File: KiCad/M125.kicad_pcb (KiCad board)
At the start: 2 copper layers, 28.9 x 13.7 mm, 20 parts, among them J1 Conn_01x04, J2 Conn_01x04, J3 Shelly, Q1 PMF250XNEX, U1 ESP32-PICO-MINI-02, U2 LMR16006+FB

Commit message: New PCB
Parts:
- added REF**: AJK, RevK:AJK, B.Cu at (88.0, 41.5)
- C3, C4, C5, D2, L1: moved to B.Cu
- moved D2 30.7 mm to (100.5, 42.3), turned to 180 degrees
- moved C3 23.5 mm to (96.2, 45.2), turned to 90 degrees
- moved L1 21.5 mm to (102.2, 45.5), turned to 180 degrees
- moved R1 13.2 mm to (112.2, 41.8), turned to 180 degrees
- moved R3 11.9 mm to (112.2, 43.2), turned to 180 degrees
- moved R5 11.2 mm to (99.6, 48.9)
- moved C5 11.2 mm to (103.7, 42.0), turned to -90 degrees
- moved R2 10.8 mm to (112.2, 44.8), turned to 180 degrees
- moved C2 10.8 mm to (94.0, 40.3), turned to 90 degrees
- moved R6 9.23 mm to (97.0, 48.9), turned to 0 degrees
- moved R4 8.25 mm to (94.9, 43.0), turned to -90 degrees
- moved C4 7.62 mm to (97.4, 42.0), turned to 90 degrees
- moved Q1 7.52 mm to (88.0, 49.5), turned to 90 degrees
- moved D1 7.22 mm to (112.2, 40.0), turned to 180 degrees
- moved C1 6.55 mm to (95.3, 47.2)
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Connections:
- U1 pad 12: unconnected-(U1-Pad12) -> DATA
- U1 pad 13: unconnected-(U1-Pad13) -> SEND
- U1 pad 18: NFCTX -> unconnected-(U1-Pad18)
- U1 pad 20: NFCRX -> unconnected-(U1-Pad20)
- U1 pad 21: DATA -> unconnected-(U1-Pad21)
- U1 pad 27: B -> NFCTX
- U1 pad 28: SEND -> NFCRX
- U1 pad 35: unconnected-(U1-Pad35) -> B
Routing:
- net +3V3: track 0.00 -> 41.0 mm, vias 0 -> 1
- net SEND: track 0.00 -> 10.8 mm, vias 0 -> 1
- net TX: track 0.00 -> 9.52 mm, vias 0 -> 1
- net B: track 0.00 -> 9.13 mm, vias 0 -> 1
- net RX: track 0.00 -> 8.70 mm, vias 0 -> 1
- net G: track 0.00 -> 8.58 mm, vias 0 -> 1
- net GPIO0: track 0.00 -> 7.65 mm
- net DC: track 0.00 -> 7.18 mm
- net NFCTX: track 0.00 -> 7.13 mm
- net R: track 0.00 -> 6.46 mm, vias 0 -> 1
- net Net-(D1-Pad3): track 0.00 -> 6.08 mm
- net EN: track 0.00 -> 4.58 mm, vias 0 -> 1
- net DATA: track 0.00 -> 4.55 mm, vias 0 -> 1
- net Net-(D1-Pad4): track 0.00 -> 4.53 mm
- net GND: track 0.00 -> 4.46 mm, vias 0 -> 1
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- added copper zone on B.Cu, net GND
- added copper zone on F.Cu, net GND
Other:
- board size 28.9 x 13.7 mm -> 29 x 13.6 mm
- board text added: "-33"
- board text added: "32"
- board text added: "3V3"
- board text added: "7"
- board text added: "8"
- board text added: "DATA"
- board text added: "DC"
- board text added: "M-125"
- board text added: "M-125 SCALES"
- board text added: "NFC"
- board text added: "NFC READER"
- board text added: "RGB: 22/19/21"
- board text added: "SEND"
- board text added: "⏚"
- board text removed: "RGB: 22/19/7"
- board text removed: "www.me.uk"

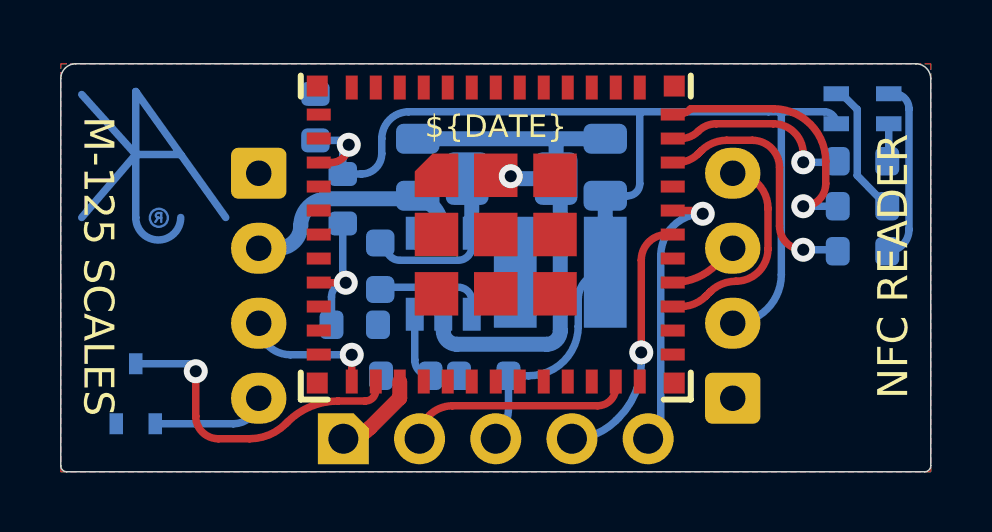
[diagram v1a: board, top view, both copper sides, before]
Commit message: Tidy PCB for placement of regulator parts
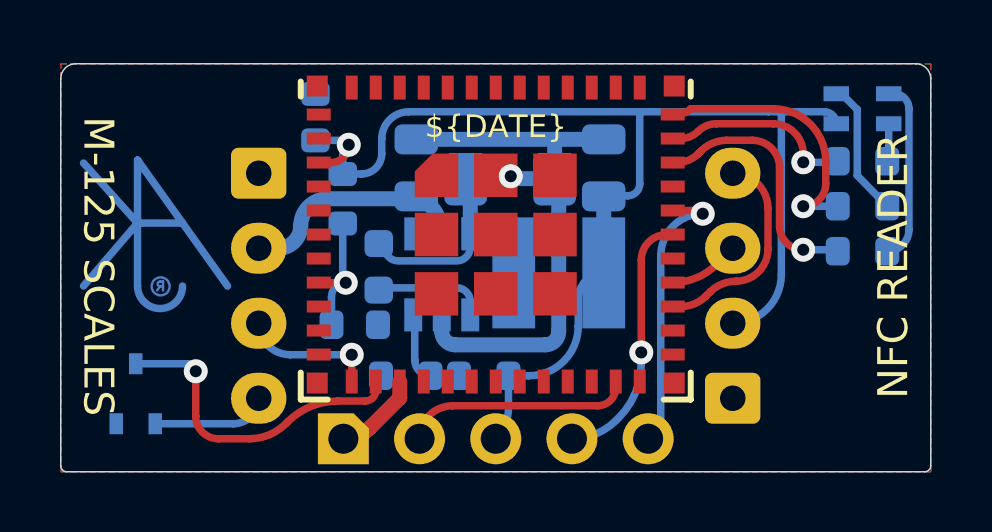
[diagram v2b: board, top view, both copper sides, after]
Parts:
- removed REF**: AJK, RevK:AJK
- added Logo1: AJK, RevK:AJK, B.Cu at (88.1, 43.8)
- C3: value 0.1uF -> 100nF; footprint RevK:Hidden -> RevK:C_0603_
- C4, C5: footprint RevK:Hidden -> RevK:C_0805_
- D2: footprint RevK:Hidden -> RevK:D_1206_
- L1: footprint RevK:Hidden -> RevK:L_4x4_
- moved C5 6.30 mm to (97.3, 42.0), turned to 90 degrees
- moved C4 6.20 mm to (103.6, 42.0)
- moved C3 0.05 mm to (96.1, 45.3)
- moved L1 0.05 mm to (102.1, 45.5), turned to 0 degrees
- moved D2 0.05 mm to (100.5, 42.4), turned to 0 degrees
- moved U2 0.05 mm to (98.2, 45.5)
